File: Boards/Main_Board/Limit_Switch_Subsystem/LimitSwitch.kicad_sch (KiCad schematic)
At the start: 7 parts, among them J20 OQ0212500000G, U17 UCLAMP3301H.TCT

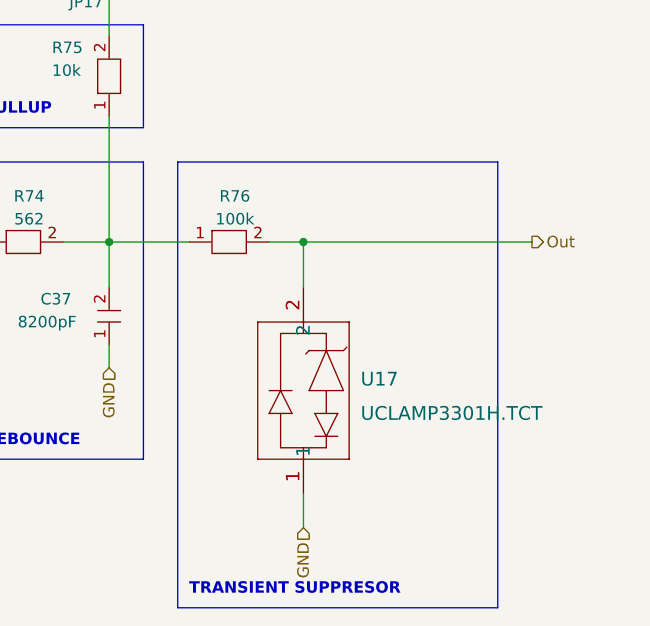
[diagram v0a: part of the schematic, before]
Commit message: Correct spacing on sensor board, refactor datasheets and project libraries
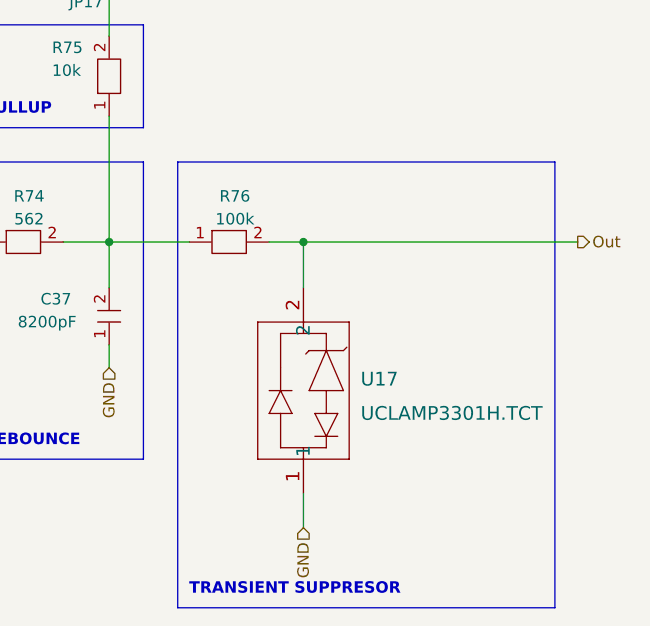
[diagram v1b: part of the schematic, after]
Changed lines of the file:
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@@
     (stroke (width 0) (type default) (color 0 0 0 0))
   )
-  (wire (pts (xy 165.1 90.17) (xy 190.5 90.17))
+  (wire (pts (xy 165.1 90.17) (xy 195.58 90.17))
     (stroke (width 0) (type default) (color 0 0 0 0))
   )
-  (polyline (pts (xy 151.13 130.81) (xy 186.69 130.81))
+  (polyline (pts (xy 151.13 130.81) (xy 193.04 130.81))
     (stroke (width 0) (type default) (color 0 0 0 0))
   )
@@
     (stroke (width 0) (type default) (color 0 0 0 0))
   )
-  (polyline (pts (xy 151.13 81.28) (xy 186.69 81.28))
+  (polyline (pts (xy 151.13 81.28) (xy 193.04 81.28))
     (stroke (width 0) (type default) (color 0 0 0 0))
   )
-  (polyline (pts (xy 186.69 130.81) (xy 186.69 81.28))
+  (polyline (pts (xy 193.04 130.81) (xy 193.04 81.28))
     (stroke (width 0) (type default) (color 0 0 0 0))
   )
@@
     (effects (font (size 1.27 1.27)) (justify right))
   )
-  (hierarchical_label "Out" (shape output) (at 190.5 90.17 0)
+  (hierarchical_label "Out" (shape output) (at 195.58 90.17 0)
     (effects (font (size 1.27 1.27)) (justify left))
   )
